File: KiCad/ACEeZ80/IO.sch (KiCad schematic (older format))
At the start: 6 parts

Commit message: Tidy up Capcitors in power supply to remove errors add labels.
Primary Development is now ACE3NOKB.


Signed-off-by: John Bradley <flypie@rocketmail.com>
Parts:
- added Z1000: Z51F3220SKX, SOIC127P1040X254-32N, symbol SamacSys_Parts:Z51F3220SKX
- added Z1001: STM8S003F3P, Package_SO:TSSOP-20_4.4x6.5mm_P0.65mm, symbol MCU_ST_STM8:STM8S003F3P
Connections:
- net labels added: I2C-Clock, I2C-Data
- wire segments 61 -> 78
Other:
- moved on the sheet: EMAC1, PIOA1, PIOB1, PS/2, SIOA1, SIOB1

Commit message: Update Post ACE4 Boards. Add MPU to eZ80 for Keyboard. Add eZ80 RAM card. Split MMU and PSU into own sub-schema.
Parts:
- removed Z1000: Z51F3220SKX, SOIC127P1040X254-32N, symbol SamacSys_Parts:Z51F3220SKX
- removed Z1001: STM8S003F3P, Package_SO:TSSOP-20_4.4x6.5mm_P0.65mm, symbol MCU_ST_STM8:STM8S003F3P
- added C1000: 1uf, Capacitor_THT:C_Disc_D3.0mm_W1.6mm_P2.50mm, symbol Device:C
- added J1000: Conn_02x06_Counter_Clockwise, Connector_PinHeader_2.54mm:PinHeader_2x06_P2.54mm_Vertical, symbol Connector_Generic:Conn_02x06_Counter_Clockwise
- added Z1100: STM8S003F3P, Package_SO:TSSOP-20_4.4x6.5mm_P0.65mm, symbol MCU_ST_STM8:STM8S003F3P
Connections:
- net labels removed: CKS, RxS\~CTS~, TRxCA, TRxCB, TxS, ~DTR~\REQA, ~RTxCA, ~RTxCB, ~SYNCA, ~SYNCB, ~W~\REQA
- wire segments 78 -> 105
- no-connect marks 4 -> 14
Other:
- moved on the sheet: PS/2

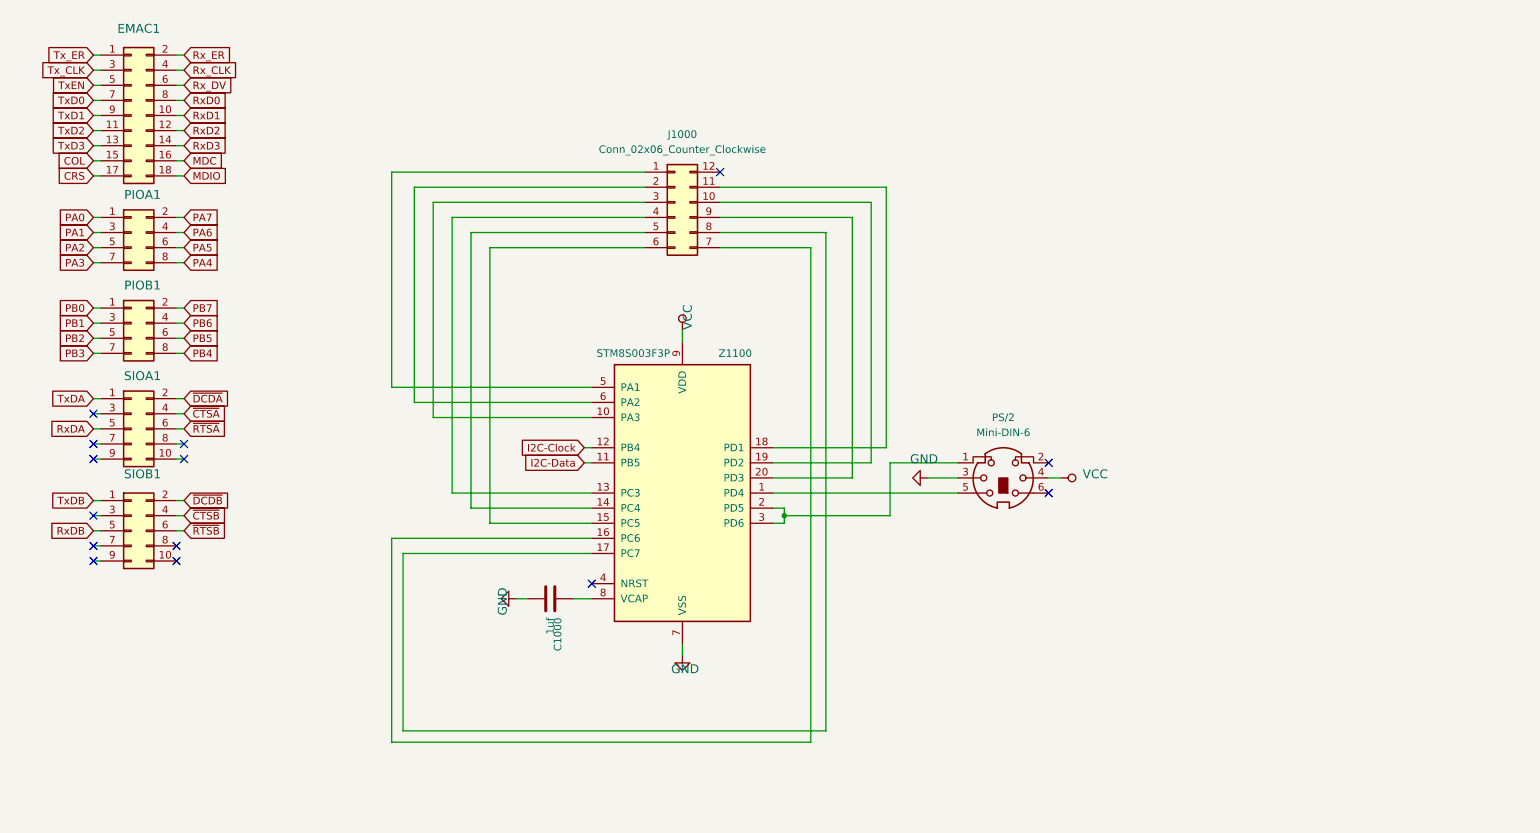
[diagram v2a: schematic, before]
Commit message: Add some outline designs for add on cards and adapters. Modify ACEeZ80 so that full address bus is on the expander slot, add I2C pins
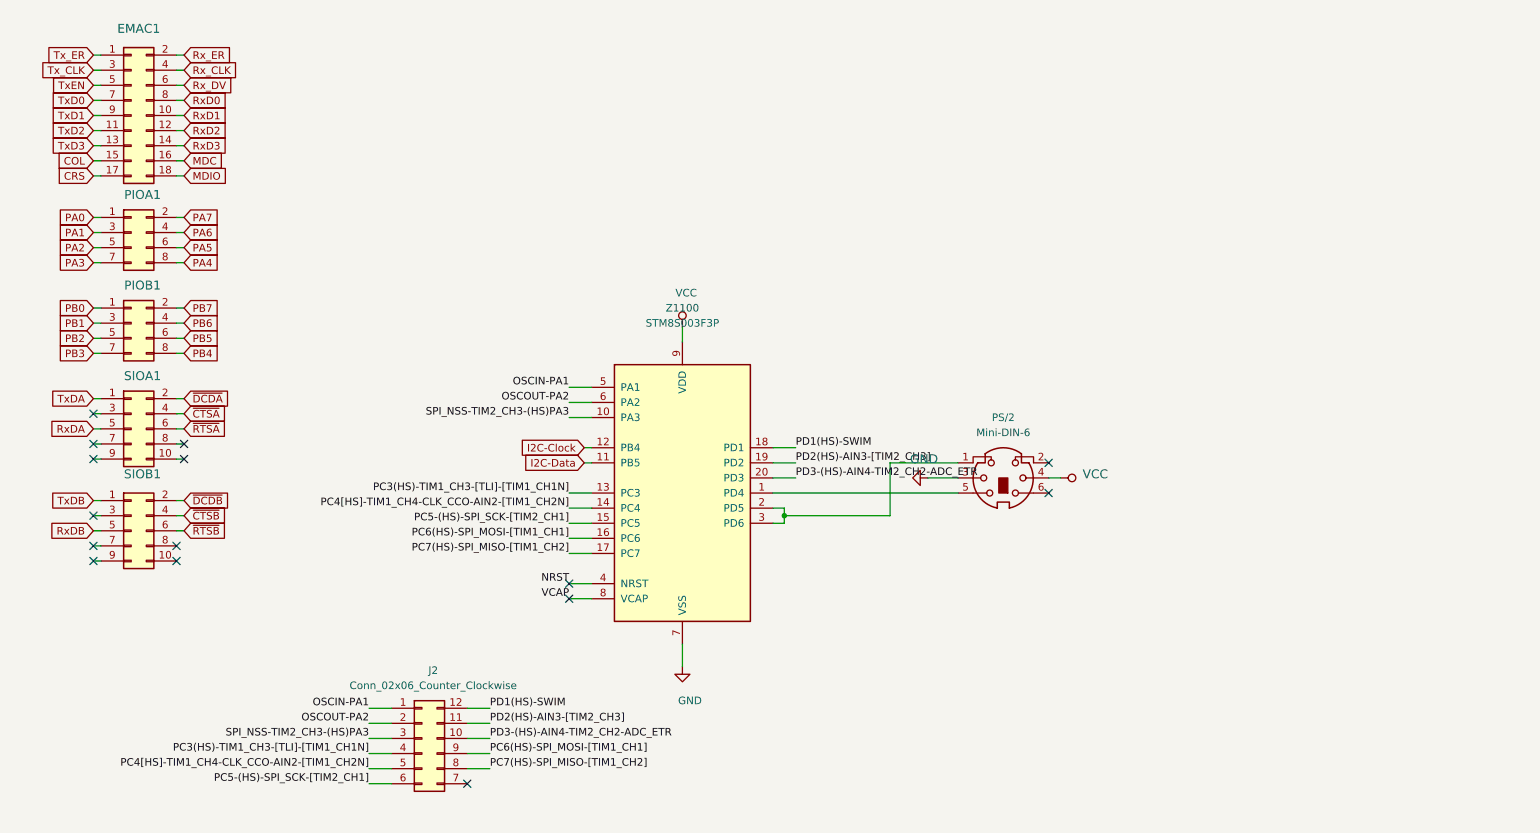
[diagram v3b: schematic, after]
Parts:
- removed C1000: 1uf, Capacitor_THT:C_Disc_D3.0mm_W1.6mm_P2.50mm, symbol Device:C
- removed J1000: Conn_02x06_Counter_Clockwise, Connector_PinHeader_2.54mm:PinHeader_2x06_P2.54mm_Vertical, symbol Connector_Generic:Conn_02x06_Counter_Clockwise
- added J2: Conn_02x06_Counter_Clockwise, Connector_PinHeader_2.54mm:PinHeader_2x06_P2.54mm_Vertical, symbol Connector_Generic:Conn_02x06_Counter_Clockwise
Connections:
- net SPI_NSS-TIM2_CH3-(HS)PA3: now reaches Z1100.10 (PA3)
- net SPI_NSS-TIM2_CH3-(HS)PA3: now also J2.3 (Pin_3)
- net PC3(HS)-TIM1_CH3-[TLI]-[TIM1_CH1N]: now reaches Z1100.13 (PC3)
- net PC3(HS)-TIM1_CH3-[TLI]-[TIM1_CH1N]: now also J2.4 (Pin_4)
- net PC4[HS]-TIM1_CH4-CLK_CCO-AIN2-[TIM1_CH2N]: now reaches Z1100.14 (PC4)
- net PC4[HS]-TIM1_CH4-CLK_CCO-AIN2-[TIM1_CH2N]: now also J2.5 (Pin_5)
- net PC5-(HS)-SPI_SCK-[TIM2_CH1]: now reaches Z1100.15 (PC5)
- net PC5-(HS)-SPI_SCK-[TIM2_CH1]: now also J2.6 (Pin_6)
- net PC6(HS)-SPI_MOSI-[TIM1_CH1]: now reaches Z1100.16 (PC6)
- net PC6(HS)-SPI_MOSI-[TIM1_CH1]: now also J2.9 (Pin_9)
- net PC7(HS)-SPI_MISO-[TIM1_CH2]: now reaches Z1100.17 (PC7)
- net PC7(HS)-SPI_MISO-[TIM1_CH2]: now also J2.8 (Pin_8)
- net PD1(HS)-SWIM: now reaches Z1100.18 (PD1)
- net PD1(HS)-SWIM: now also J2.12 (Pin_12)
- net PD2(HS)-AIN3-[TIM2_CH3]: now reaches Z1100.19 (PD2)
- net PD2(HS)-AIN3-[TIM2_CH3]: now also J2.11 (Pin_11)
- net PD3-(HS)-AIN4-TIM2_CH2-ADC_ETR: now reaches Z1100.20 (PD3)
- net PD3-(HS)-AIN4-TIM2_CH2-ADC_ETR: now also J2.10 (Pin_10)
- net NRST: now reaches Z1100.4 (NRST)
- net OSCIN-PA1: now reaches Z1100.5 (PA1)
- net OSCIN-PA1: now also J2.1 (Pin_1)
- net OSCOUT-PA2: now reaches Z1100.6 (PA2)
- net OSCOUT-PA2: now also J2.2 (Pin_2)
- net VCAP: now reaches Z1100.8 (VCAP)
- no-connect marks 14 -> 15
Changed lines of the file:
@@
 U 1 1 5DC55916
 P 5100 3575
-F 0 "Z1100" H 5450 4500 50  0000 C CNN
-F 1 "STM8S003F3P" H 4775 4500 50  0000 C CNN
+F 0 "Z1100" H 5100 4800 50  0000 C CNN
+F 1 "STM8S003F3P" H 5100 4700 50  0000 C CNN
 F 2 "Package_SO:TSSOP-20_4.4x6.5mm_P0.65mm" H 5150 4675 50  0001 L CNN
 F 3 "http://www.st.com/st-web-ui/static/active/en/resource/technical/document/datasheet/DM00024550.pdf" H 5050 3175 50  0001 C CNN
@@
 Connection ~ 5775 3725
 Wire Wire Line
-	5100 2495 5100 2575
+	5100 4575 5100 4725
 $Comp
-L power:VCC #
-U 1 1 5DC8032B
-P 5100 2495
-AR Path="/5DC8032B" Ref="#"  Part="P+?"
-AR Path="/5D9DD1F0/5DC8032B" Ref="#0168"  Part="1"
-F 0 "#0168" H 5100 2495 50  0001 C CNN
-F 1 "VCC" V 5100 2495 59  0000 L BNN
-F 2 "" H 5100 2495 50  0001 C CNN
-F 3 "" H 5100 2495 50  0001 C CNN
-	1    5100 2495
-	-1   0    0    -1
+L power:GND #PWR0102
+U 1 1 5DD55A85
+P 5100 4725
+F 0 "#PWR0102" H 5100 4475 50  0001 C CNN
+F 1 "GND" H 5150 4500 50  0000 C CNN
+F 2 "" H 5100 4725 50  0001 C CNN
+F 3 "" H 5100 4725 50  0001 C CNN
+	1    5100 4725
+	1    0    0    -1
 $EndComp
 $Comp
-L power:GND #
-U 1 1 5DC868D4
-P 5100 4650
-AR Path="/5DC868D4" Ref="#"  Part="SUPPLY?"
-AR Path="/5D9DD1F0/5DC868D4" Ref="#0169"  Part="1"
-F 0 "#0169" H 5100 4650 50  0001 C CNN
-F 1 "GND" H 5025 4525 59  0000 L BNN
-F 2 "" H 5100 4650 50  0001 C CNN
-F 3 "" H 5100 4650 50  0001 C CNN
-	1    5100 4650
+L power:VCC #PWR0103
+U 1 1 5DD58AFC
+P 5100 2475
+F 0 "#PWR0103" H 5100 2325 50  0001 C CNN
+F 1 "VCC" H 5125 2700 50  0000 C CNN
+F 2 "" H 5100 2475 50  0001 C CNN
+F 3 "" H 5100 2475 50  0001 C CNN
+	1    5100 2475
 	1    0    0    -1
 $EndComp
 Wire Wire Line
-	5100 4575 5100 4650
+	5100 2475 5100 2575
 Text GLabel 4450 3275 0    50   Input ~ 0
 I2C-Clock
@@
 Wire Wire Line
 	4500 3375 4450 3375
-NoConn ~ 4500 4175
+Wire Wire Line
+	4500 2875 4350 2875
+Text Label 4350 2875 2    50   ~ 0
+OSCIN-PA1
+Wire Wire Line
+	4500 2975 4350 2975
+Text Label 4350 2975 2    50   ~ 0
+OSCOUT-PA2
+Wire Wire Line
+	4500 3075 4350 3075
+Text Label 4350 3075 2    50   ~ 0
+SPI_NSS-TIM2_CH3-(HS)PA3
+Wire Wire Line
+	4500 3575 4350 3575
+Text Label 4350 3575 2    50   ~ 0
+PC3(HS)-TIM1_CH3-[TLI]-[TIM1_CH1N]
+Wire Wire Line
+	4500 3675 4350 3675
+Text Label 4350 3675 2    50   ~ 0
+PC4[HS]-TIM1_CH4-CLK_CCO-AIN2-[TIM1_CH2N]
+Wire Wire Line
+	4500 3775 4350 3775
+Text Label 4350 3775 2    50   ~ 0
+PC5-(HS)-SPI_SCK-[TIM2_CH1]
+Wire Wire Line
+	4500 3975 4350 3975
+Text Label 4350 3975 2    50   ~ 0
+PC7(HS)-SPI_MISO-[TIM1_CH2]
+Wire Wire Line
+	4500 3875 4350 3875
+Text Label 4350 3875 2    50   ~ 0
+PC6(HS)-SPI_MOSI-[TIM1_CH1]
+Wire Wire Line
+	4500 4175 4350 4175
+Text Label 4350 4175 2    50   ~ 0
+NRST
+Wire Wire Line
+	4500 4275 4350 4275
+Text Label 4350 4275 2    50   ~ 0
+VCAP
+Wire Wire Line
+	5700 3275 5850 3275
+Text Label 5850 3275 0    50   ~ 0
+PD1(HS)-SWIM
+Wire Wire Line
+	5700 3375 5850 3375
+Text Label 5850 3375 0    50   ~ 0
+PD2(HS)-AIN3-[TIM2_CH3]
+Wire Wire Line
+	5700 3475 5850 3475
+Text Label 5850 3475 0    50   ~ 0
+PD3-(HS)-AIN4-TIM2_CH2-ADC_ETR
 $Comp
-L Device:C C1000
-U 1 1 5DCA9033
-P 4225 4275
-F 0 "C1000" H 4350 4325 50  0000 L CNN
-F 1 "1uf" H 4350 4275 50  0000 L CNN
-F 2 "Capacitor_THT:C_Disc_D3.0mm_W1.6mm_P2.50mm" H 4263 4125 50  0001 C CNN
-F 3 "~" H 4225 4275 50  0001 C CNN
-	1    4225 4275
-	0    1    1    0
-$EndComp
-$Comp
-L power:GND #
-U 1 1 5DCAA50B
-P 4000 4275
-AR Path="/5DCAA50B" Ref="#"  Part="SUPPLY?"
-AR Path="/5D9DD1F0/5DCAA50B" Ref="#0170"  Part="1"
-F 0 "#0170" H 4000 4275 50  0001 C CNN
-F 1 "GND" H 3925 4150 59  0000 L BNN
-F 2 "" H 4000 4275 50  0001 C CNN
-F 3 "" H 4000 4275 50  0001 C CNN
-	1    4000 4275
-	0    1    1    0
-$EndComp
-Wire Wire Line
-	4075 4275 4000 4275
-$Comp
-L Connector_Generic:Conn_02x06_Counter_Clockwise J1000
-U 1 1 5DD0638C
-P 5050 1650
-F 0 "J1000" H 5100 2100 50  0000 C CNN
-F 1 "Conn_02x06_Counter_Clockwise" H 5100 2000 50  0000 C CNN
-F 2 "Connector_PinHeader_2.54mm:PinHeader_2x06_P2.54mm_Vertical" H 5050 1650 50  0001 C CNN
-F 3 "~" H 5050 1650 50  0001 C CNN
-	1    5050 1650
+L Connector_Generic:Conn_02x06_Counter_Clockwise J2
+U 1 1 5DDA3286
+P 3375 5200
+F 0 "J2" H 3450 5650 50  0000 C CNN
+F 1 "Conn_02x06_Counter_Clockwise" H 3450 5550 50  0000 C CNN
+F 2 "Connector_PinHeader_2.54mm:PinHeader_2x06_P2.54mm_Vertical" H 3375 5200 50  0001 C CNN
+F 3 "~" H 3375 5200 50  0001 C CNN
+	1    3375 5200
 	1    0    0    -1
 $EndComp
 Wire Wire Line
-	4500 2975 3325 2975
+	3175 5000 3025 5000
+Text Label 3025 5000 2    50   ~ 0
+OSCIN-PA1
 Wire Wire Line
-	4500 3075 3450 3075
+	3175 5100 3025 5100
+Text Label 3025 5100 2    50   ~ 0
+OSCOUT-PA2
 Wire Wire Line
-	4500 2875 3175 2875
+	3175 5200 3025 5200
+Text Label 3025 5200 2    50   ~ 0
+SPI_NSS-TIM2_CH3-(HS)PA3
 Wire Wire Line
-	4850 1450 3175 1450
+	3675 5000 3825 5000
+Text Label 3825 5000 0    50   ~ 0
+PD1(HS)-SWIM
 Wire Wire Line
-	3175 1450 3175 2875
+	3675 5100 3825 5100
+Text Label 3825 5100 0    50   ~ 0
+PD2(HS)-AIN3-[TIM2_CH3]
 Wire Wire Line
-	4850 1550 3325 1550
+	3675 5200 3825 5200
+Text Label 3825 5200 0    50   ~ 0
+PD3-(HS)-AIN4-TIM2_CH2-ADC_ETR
 Wire Wire Line
-	3325 1550 3325 2975
+	3175 5300 3025 5300
+Text Label 3025 5300 2    50   ~ 0
+PC3(HS)-TIM1_CH3-[TLI]-[TIM1_CH1N]
 Wire Wire Line
-	4850 1650 3450 1650
+	3175 5400 3025 5400
+Text Label 3025 5400 2    50   ~ 0
+PC4[HS]-TIM1_CH4-CLK_CCO-AIN2-[TIM1_CH2N]
 Wire Wire Line
-	3450 1650 3450 3075
+	3175 5500 3025 5500
+Text Label 3025 5500 2    50   ~ 0
+PC5-(HS)-SPI_SCK-[TIM2_CH1]
 Wire Wire Line
-	3575 3575 3575 1750
+	3675 5400 3825 5400
+Text Label 3825 5400 0    50   ~ 0
+PC7(HS)-SPI_MISO-[TIM1_CH2]
 Wire Wire Line
-	3575 1750 4850 1750
-Wire Wire Line
-	3575 3575 4500 3575
-Wire Wire Line
-	3700 3675 3700 1850
-Wire Wire Line
-	3700 1850 4850 1850
-Wire Wire Line
-	3700 3675 4500 3675
-Wire Wire Line
-	4500 3775 3825 3775
-Wire Wire Line
-	3825 3775 3825 1950
-Wire Wire Line
-	3825 1950 4850 1950
-Wire Wire Line
-	4375 4275 4500 4275
-Wire Wire Line
-	4500 3875 3175 3875
-Wire Wire Line
-	3175 3875 3175 5225
-Wire Wire Line
-	3175 5225 5950 5225
-Wire Wire Line
-	5950 5225 5950 1950
-Wire Wire Line
-	5950 1950 5350 1950
-Wire Wire Line
-	4500 3975 3250 3975
-Wire Wire Line
-	3250 3975 3250 5150
-Wire Wire Line
-	3250 5150 6050 5150
-Wire Wire Line
-	6050 5150 6050 1850
-Wire Wire Line
-	6050 1850 5350 1850
-Wire Wire Line
-	5700 3475 6225 3475
-Wire Wire Line
-	6225 3475 6225 1750
-Wire Wire Line
-	6225 1750 5350 1750
-Wire Wire Line
-	5700 3375 6350 3375
-Wire Wire Line
-	6350 3375 6350 1650
-Wire Wire Line
-	6350 1650 5350 1650
-Wire Wire Line
-	6450 1550 5350 1550
-NoConn ~ 5350 1450
-Wire Wire Line
-	5700 3275 6450 3275
-Wire Wire Line
-	6450 1550 6450 3275
+	3675 5300 3825 5300
+Text Label 3825 5300 0    50   ~ 0
+PC6(HS)-SPI_MOSI-[TIM1_CH1]
+NoConn ~ 4350 4275
+NoConn ~ 4350 4175
+NoConn ~ 3675 5500
 $EndSCHEMATC
